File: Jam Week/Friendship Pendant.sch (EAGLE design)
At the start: 33 parts, among them IC1 LM556D, IC2 LM556D, IC3 74AHC1G32DCK

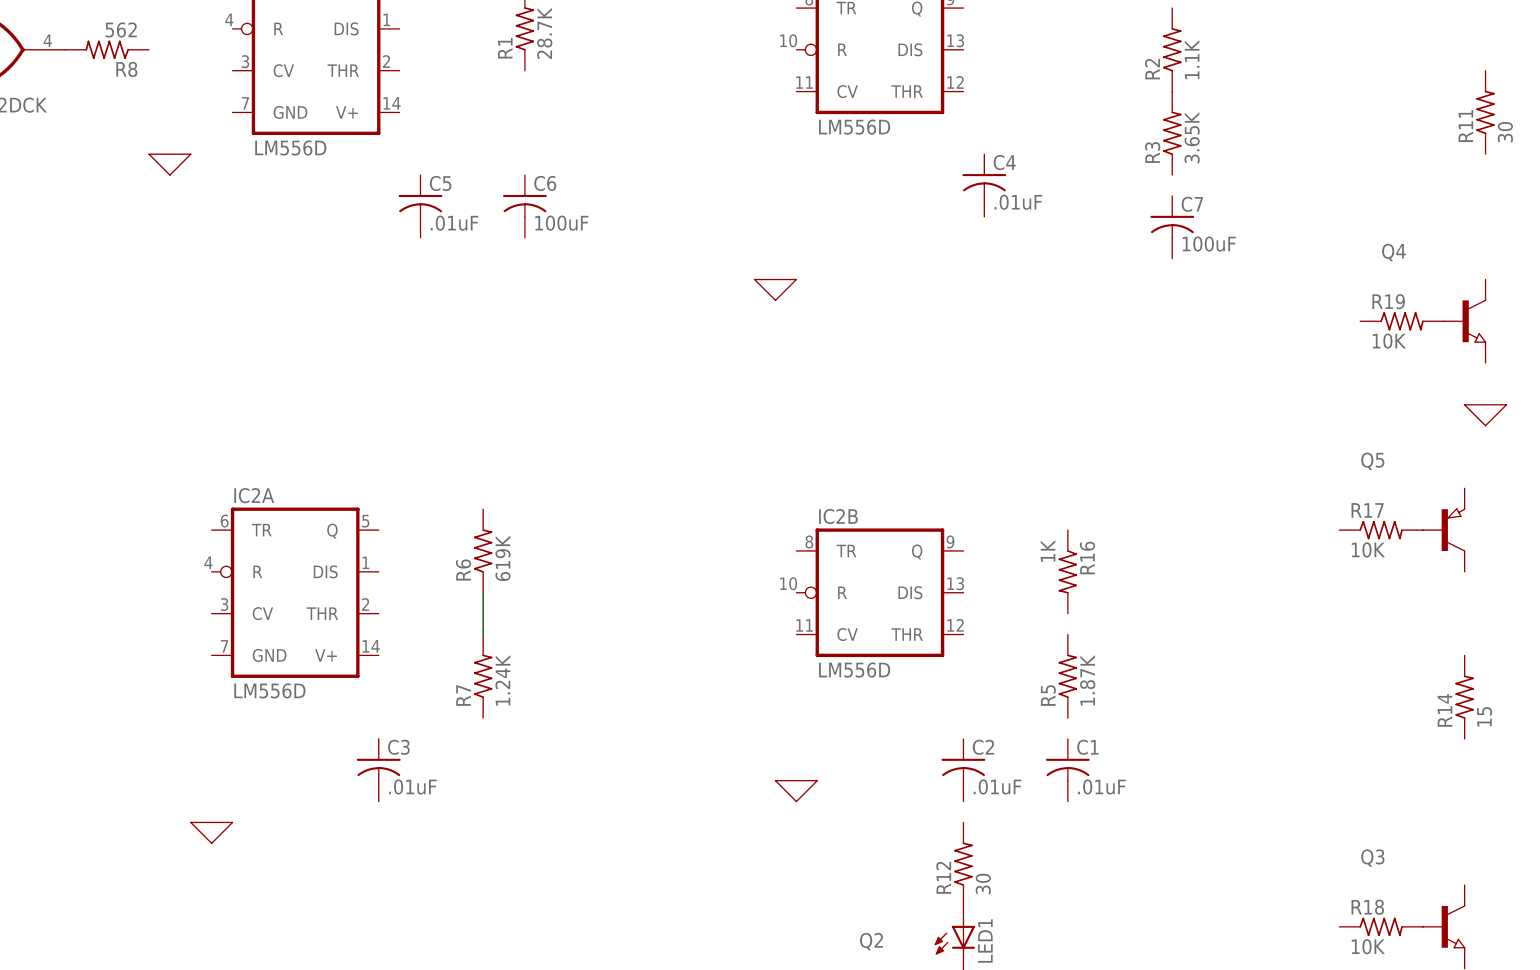
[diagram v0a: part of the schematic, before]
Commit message: Added LEDs
db
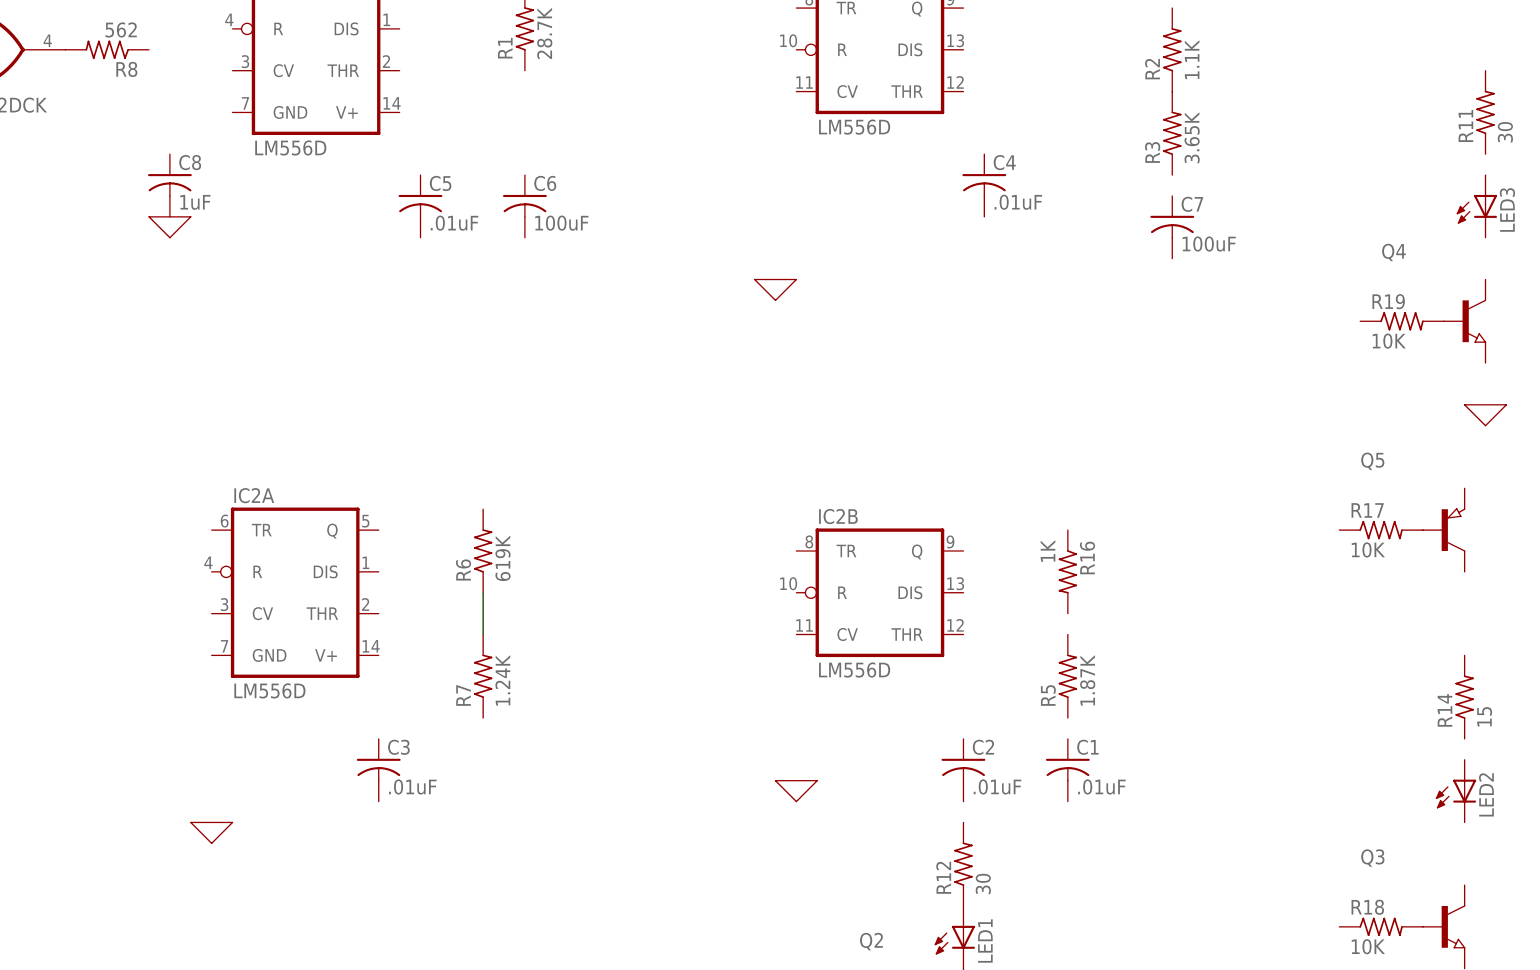
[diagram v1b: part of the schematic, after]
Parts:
- added C8: 1uF, rcl:C-USC0805
- added LED2, LED3: (no value), led:LED5MM
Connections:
- new net 0: C8.2
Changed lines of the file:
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@@
 <part name="LED1" library="led" library_urn="urn:adsk.eagle:library:259" deviceset="LED" device="IRL80A" package3d_urn="urn:adsk.eagle:package:15810/1">
 <attribute name="MOUSER#" value="782-TSAL6200"/>
-<attribute name="MPN" value="
-TSAL6200"/>
+<attribute name="MPN" value=" TSAL6200"/>
 </part>
 <part name="X_1" library="ngspice-simulation" library_urn="urn:adsk.eagle:library:527439" deviceset="GND" device=""/>
@@
 <part name="X_7" library="ngspice-simulation" library_urn="urn:adsk.eagle:library:527439" deviceset="GND" device=""/>
 <part name="X_8" library="ngspice-simulation" library_urn="urn:adsk.eagle:library:527439" deviceset="GND" device=""/>
+<part name="LED2" library="led" library_urn="urn:adsk.eagle:library:259" deviceset="LED" device="5MM" package3d_urn="urn:adsk.eagle:package:15799/2">
+<attribute name="MOUSER#" value="859-LTL-307GLC"/>
+<attribute name="MPN" value="LTL-307GLC"/>
+</part>
+<part name="LED3" library="led" library_urn="urn:adsk.eagle:library:259" deviceset="LED" device="5MM" package3d_urn="urn:adsk.eagle:package:15799/2">
+<attribute name="MOUSER#" value="645-521-9672F"/>
+<attribute name="MPN" value="521-9672F"/>
+</part>
+<part name="C8" library="rcl" library_urn="urn:adsk.eagle:library:334" deviceset="C-US" device="C0805" package3d_urn="urn:adsk.eagle:package:23617/2" value="1uF">
+<spice>
+<pinmapping spiceprefix="C">
+<pinmap gate="G$1" pin="1" pinorder="1"/>
+<pinmap gate="G$1" pin="2" pinorder="2"/>
+</pinmapping>
+</spice>
+<attribute name="MOUSER#" value="963-JMK105BJ105KV-F"/>
+<attribute name="MPN" value="JMK105BJ105KV-F"/>
+</part>
 </parts>
 <sheets>
@@
 </instance>
 <instance part="X_1" gate="G$1" x="7.62" y="10.16" smashed="yes"/>
-<instance part="X_2" gate="G$1" x="43.18" y="40.64" smashed="yes"/>
+<instance part="X_2" gate="G$1" x="43.18" y="33.02" smashed="yes"/>
 <instance part="X_3" gate="G$1" x="48.26" y="-40.64" smashed="yes"/>
 <instance part="X_4" gate="G$1" x="119.38" y="-35.56" smashed="yes"/>
@@
 <instance part="X_7" gate="G$1" x="200.66" y="-68.58" smashed="yes"/>
 <instance part="X_8" gate="G$1" x="203.2" y="10.16" smashed="yes"/>
+<instance part="LED2" gate="G$1" x="200.66" y="-35.56" smashed="yes">
+<attribute name="NAME" x="204.216" y="-40.132" size="1.778" layer="95" rot="R90"/>
+<attribute name="VALUE" x="206.375" y="-40.132" size="1.778" layer="96" rot="R90"/>
+<attribute name="MOUSER#" x="200.66" y="-35.56" size="1.778" layer="96" display="off"/>
+<attribute name="MPN" x="200.66" y="-35.56" size="1.778" layer="96" display="off"/>
+</instance>
+<instance part="LED3" gate="G$1" x="203.2" y="35.56" smashed="yes">
+<attribute name="NAME" x="206.756" y="30.988" size="1.778" layer="95" rot="R90"/>
+<attribute name="VALUE" x="208.915" y="30.988" size="1.778" layer="96" rot="R90"/>
+<attribute name="MOUSER#" x="203.2" y="35.56" size="1.778" layer="96" display="off"/>
+<attribute name="MPN" x="203.2" y="35.56" size="1.778" layer="96" display="off"/>
+</instance>
+<instance part="C8" gate="G$1" x="43.18" y="38.1" smashed="yes">
+<attribute name="NAME" x="44.196" y="38.735" size="1.778" layer="95"/>
+<attribute name="VALUE" x="44.196" y="33.909" size="1.778" layer="96"/>
+<attribute name="MOUSER#" x="43.18" y="38.1" size="1.778" layer="96" display="off"/>
+<attribute name="MPN" x="43.18" y="38.1" size="1.778" layer="96" display="off"/>
+</instance>
 </instances>
 <busses>
@@
 </segment>
 </net>
+<net name="0" class="0">
+<segment>
+<pinref part="X_2" gate="G$1" pin="0"/>
+<pinref part="C8" gate="G$1" pin="2"/>
+</segment>
+</net>

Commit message: Almost done with eagle scematic
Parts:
- added C9: 4.7uF, rcl:C-USC0805
- added IR1: TSOP1730TB1, telefunken:TSOP1730TB1
- C8: MOUSER# 963-JMK105BJ105KV-F -> 80-C0805C105K3R; MPN JMK105BJ105KV-F -> C0805C105K3R
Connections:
- new net BLINK: IC1B.Q
- new net ENABLE: IC1A.Q, IC1B.R, R18.1
- new net N$11: IC3A.I0, IR1.VO
- new net N$12: Q1.B, R10.2
- new net N$13: IC2A.Q, R10.1
- new net N$14: C3.1, IC2A.CV
- new net N$15: IC2A.V+, R6.2
- new net N$16: C9.1, IC2A.THR, IC2A.TR, R7.1
- new net N$17: C8.1, IC1A.TR, R8.1
- new net N$18: C5.1, IC1A.CV
- new net N$19: C6.1, IC1A.DIS, IC1A.THR, R1.1
- new net N$20: R12.2
- new net N$21: IC1A.V+, R1.2
- new net N$22: IC1A.R
- new net N$23: C4.1, IC1B.CV
- new net N$24: C7.1, IC1B.THR, IC1B.TR, R3.1
- new net N$25: R2.2
- new net N$26: R19.1
- new net N$27: LED3.A, R11.1
- new net N$28: LED3.C, Q4.C
- new net N$29: Q5.C, R14.2
- new net N$30: LED2.A, R14.1
- new net N$31: LED2.C, Q3.C
- new net N$32: R17.1
- new net N$33: Q5.E
- new net N$34: C2.1, IC2B.CV
- new net N$35: C1.1, IC2B.THR, IC2B.TR, R5.1
- new net N$36: IC2B.DIS, R16.2, R5.2
- new net N$37: R16.1
- new net N$38: R11.2
- new net SIGNAL: IC2B.Q, R4.1
- new net VCC: IR1.VS
- net 0: now also C1.2, C2.2, C3.2, C4.2, C5.2, C6.2, C7.2, C9.2, IC1A.GND, IC2A.GND, IR1.GND, Q1.E, Q2.E, Q3.E, Q4.E
- net N$1: now also IC1B.DIS
- net N$2: now also IC2A.DIS
- net N$4: now also IC2B.R, IC3A.I1
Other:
- moved on the sheet: C1, C2, C3, C4, C5, C6, C7, C8, IC1B, IC2A, IC2B, IC3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

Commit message: Working on  layout
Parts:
- added TP1, TP2: TEST-POINTTP_15TH_THRU, SparkFun-Connectors:TEST-POINTTP_15TH_THRU
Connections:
- new net N$39: TP1.1
- net 0: now also TP2.1
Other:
- note added: "2xAAA Batteries"

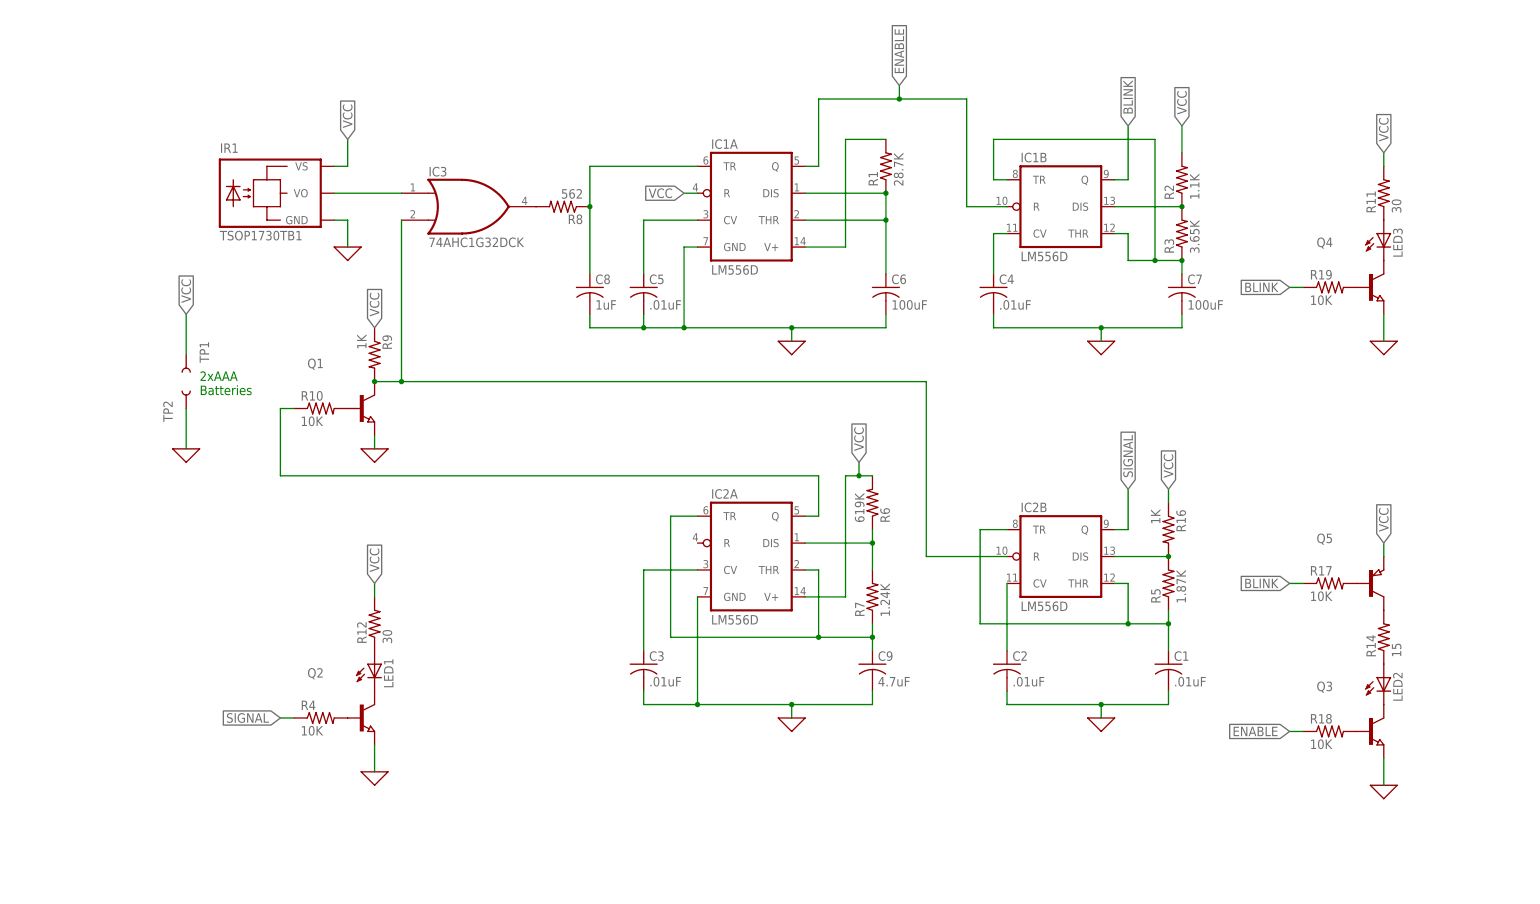
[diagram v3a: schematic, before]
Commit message: Next class resolve air wire
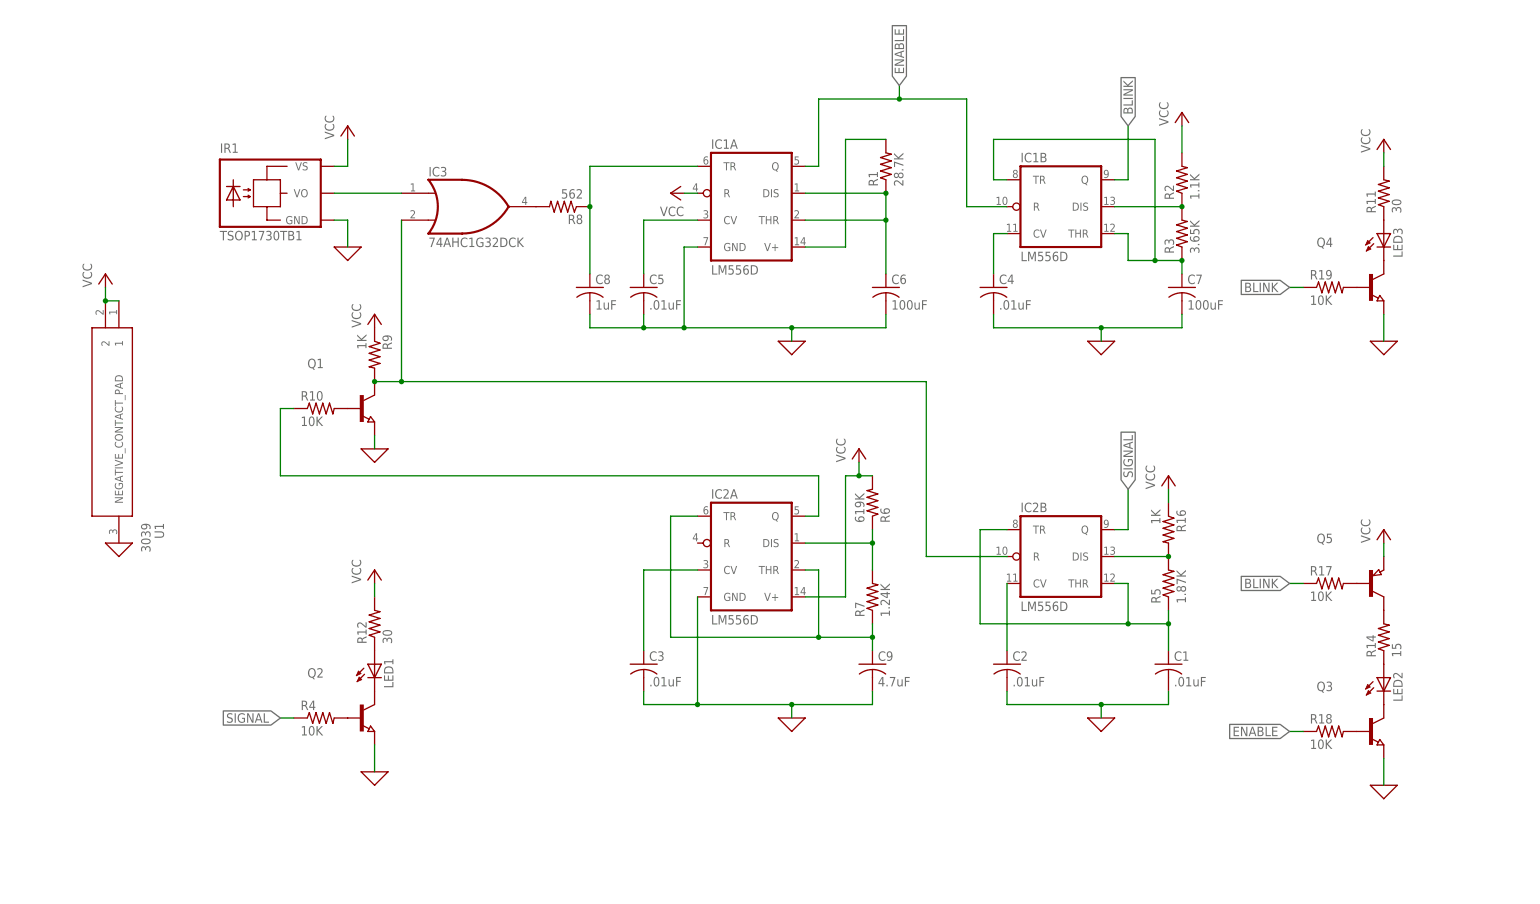
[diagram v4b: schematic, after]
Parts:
- removed TP1, TP2: TEST-POINTTP_15TH_THRU, SparkFun-Connectors:TEST-POINTTP_15TH_THRU
- added U1: 3039, 3039:3039
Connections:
- removed net N$15: IC2A.V+, R6.2
- removed net N$20: R12.2
- removed net N$22: IC1A.R
- removed net N$25: R2.2
- removed net N$33: Q5.E
- removed net N$37: R16.1
- removed net N$38: R11.2
- removed net N$39: TP1.1
- net 0: now also U1.NEGATIVE_CONTACT_PAD; no longer TP2.1
- net VCC: now also IC1A.R, IC2A.V+, Q5.E, R11.2, R12.2, R16.1, R2.2, R6.2, R9.1, U1.1, U1.2
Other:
- note removed: "2xAAA Batteries"
